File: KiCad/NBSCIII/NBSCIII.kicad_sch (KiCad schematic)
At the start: 9 parts, among them P1 CONN_1, P2 CONN_1, P3 CONN_1, P4 CONN_1

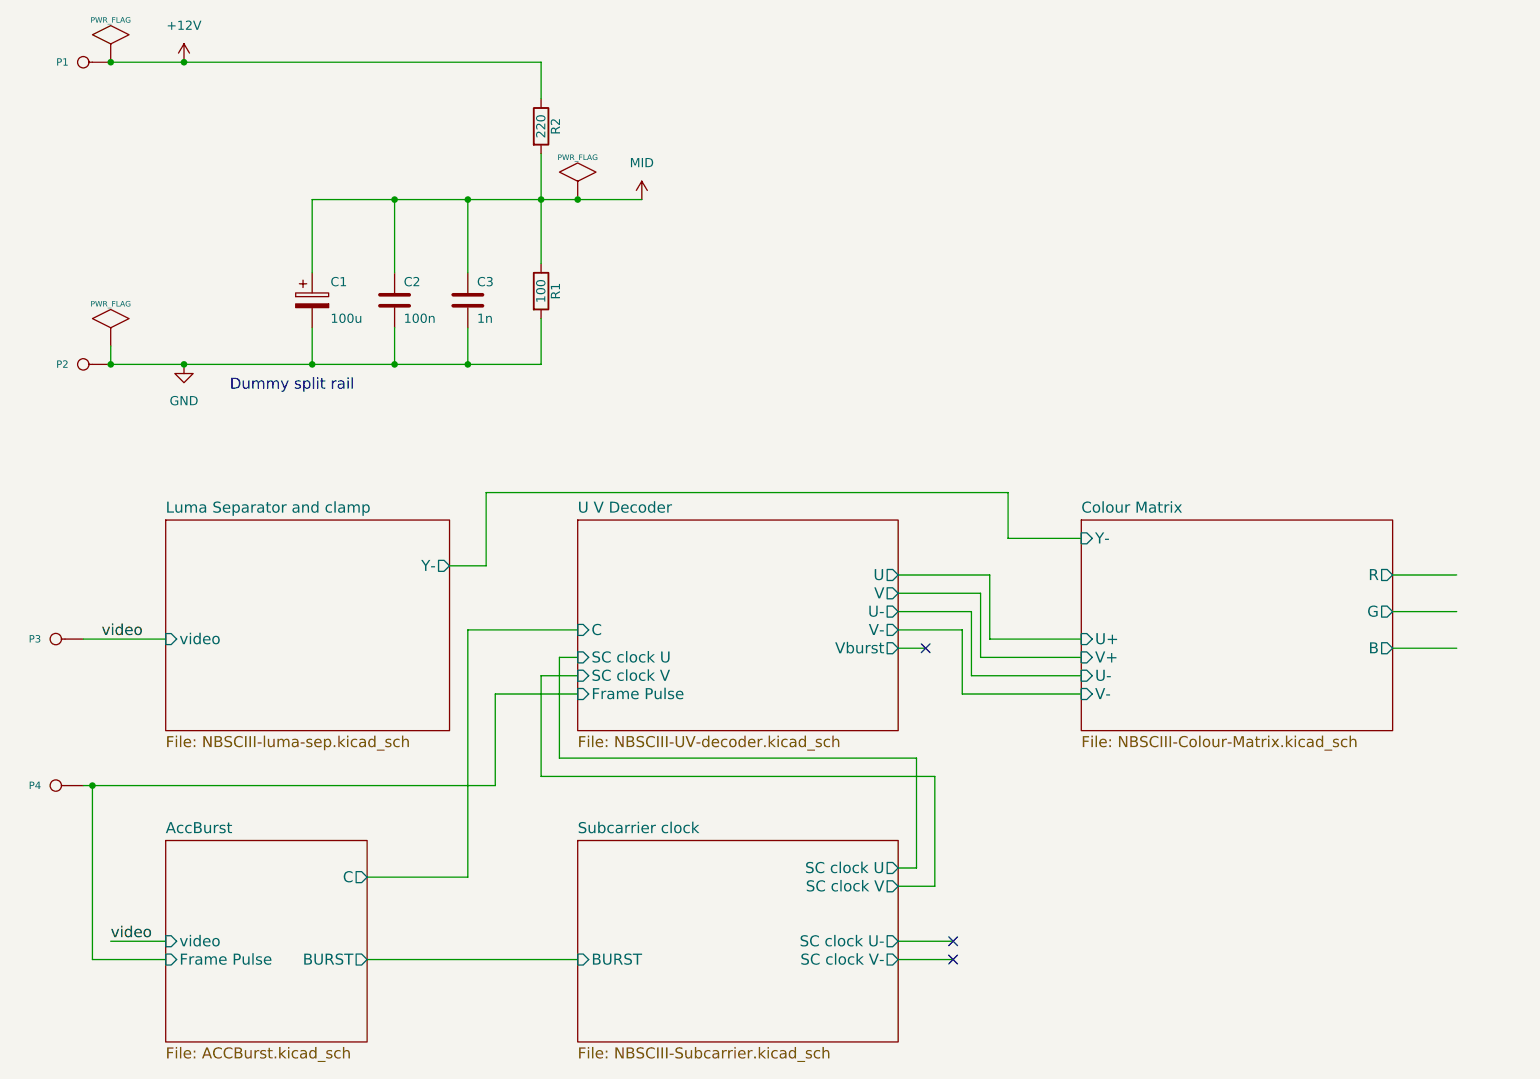
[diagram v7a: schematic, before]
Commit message: derescue connectors and pwr flags
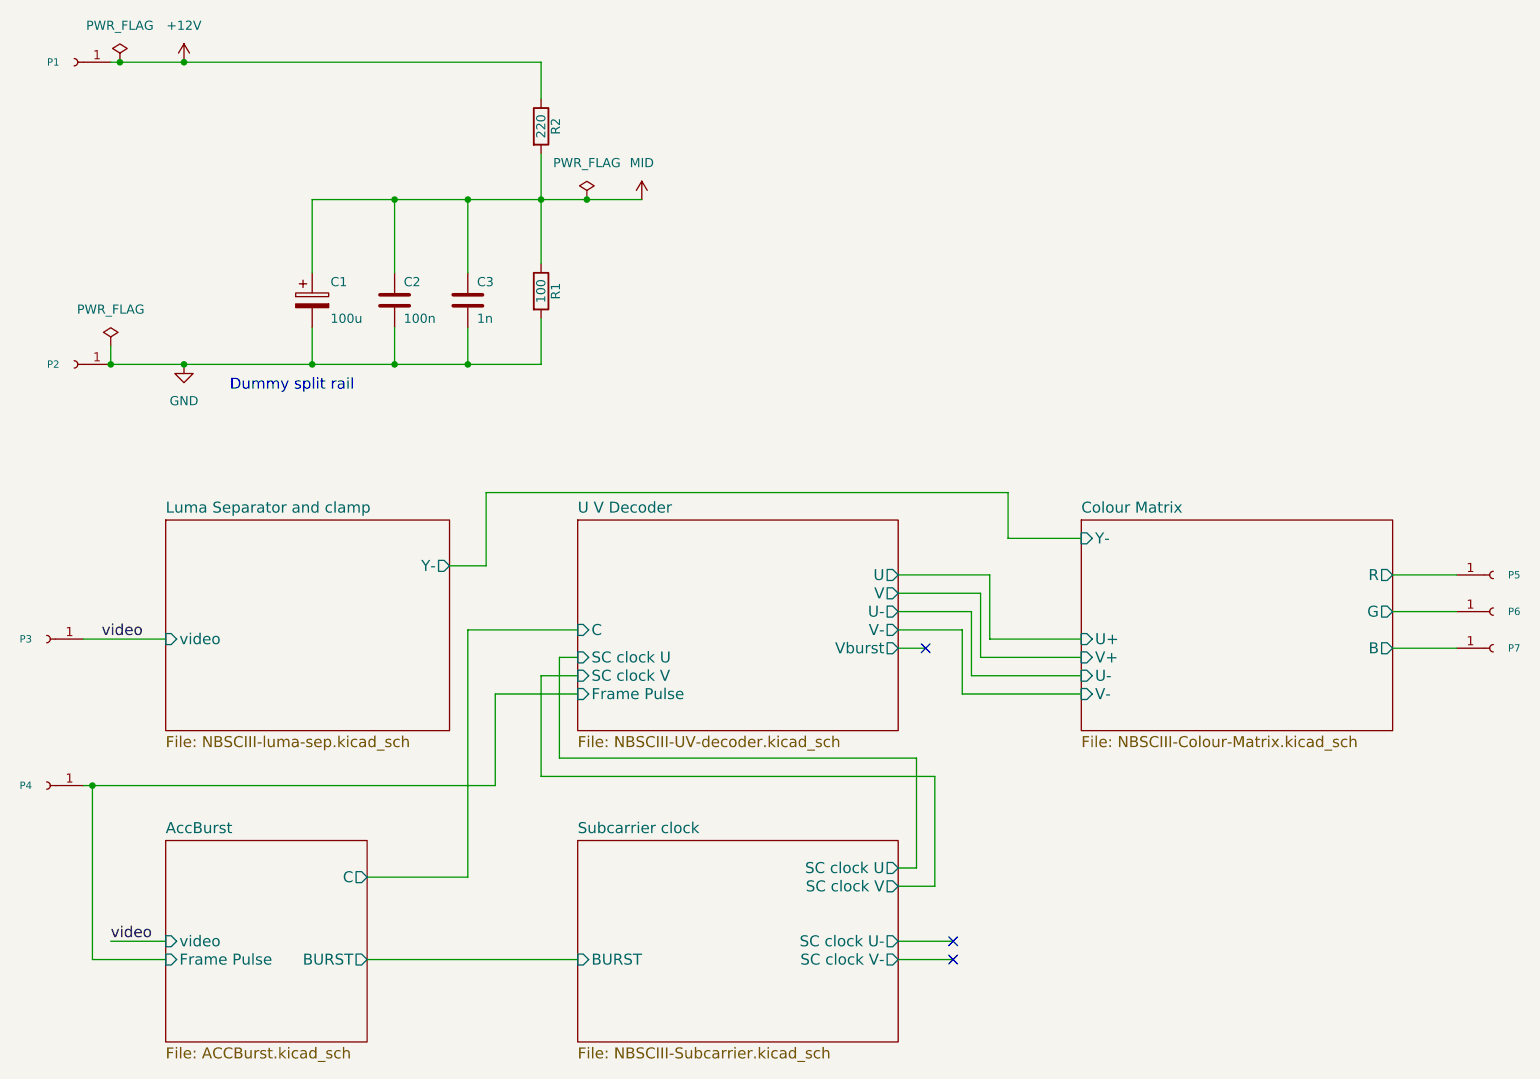
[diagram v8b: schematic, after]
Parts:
- added P5, P6, P7: Conn_01x01_Female, symbol Connector:Conn_01x01_Female
- P1, P2, P3, P4: value CONN_1 -> Conn_01x01_Female; symbol NBSCIII-rescue:CONN_1 -> Connector:Conn_01x01_Female
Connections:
- net Colour Matrix/B: now also P7.1 (Pin_1)
- net Colour Matrix/G: now also P6.1 (Pin_1)
- net Colour Matrix/R: now also P5.1 (Pin_1)
